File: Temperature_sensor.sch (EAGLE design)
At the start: 3 parts, among them J1 4_PIN_2MM

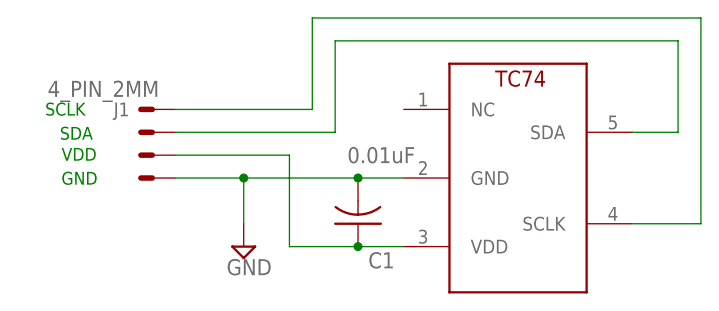
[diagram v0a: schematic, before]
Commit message: Finished Laser_Array next versions, all theee boards, Nov19_2018
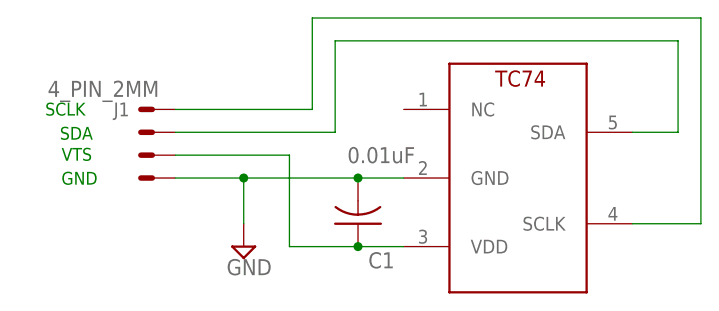
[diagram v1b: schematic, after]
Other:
- note added: "VTS"
- note removed: "VDD"
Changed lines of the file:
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@@
 <text x="-11.9" y="62.82" size="1.4224" layer="91">SCLK</text>
 <text x="-10.1" y="55.14" size="1.4224" layer="91">GND</text>
-<text x="-10.08" y="57.8" size="1.4224" layer="91">VDD</text>
+<text x="-10.08" y="57.8" size="1.4224" layer="91">VTS</text>
 </plain>
 <instances>
